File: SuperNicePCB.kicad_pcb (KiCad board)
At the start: 4 copper layers, 100 x 100 mm, 59 parts, among them J1 UART Debug, J2 Boot Opt, SW1 Reset, U1 ESP32-S3-WROOM-1-N8, U2 SY8089AAAC, U3 SGM2048-ADJXTEK8G/TR, U4 ICS-43434_C5656610, U5 AM312, U6 SCD40-D-R1, U7 SHT40-AD1B-R3, U8 HLK-LD6002, U9 DWM3000TR13

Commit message: Problems
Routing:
- net /HumanSesors/3.3V: track 299.4 -> 109.6 mm
- net /MCU/VDD33: track 131.2 -> 32.9 mm
- net /MCU/BOOT: track 77.2 -> 25.7 mm, vias 1 -> 0
- net GND: track 331.5 -> 298.1 mm, vias 35 -> 31
- net /PIR_OUT: track 32.9 -> 29.1 mm
- net /TEMP_SCL: track 75.8 -> 74.3 mm
- removed copper zone on In2.Cu, net /HumanSesors/3.3V

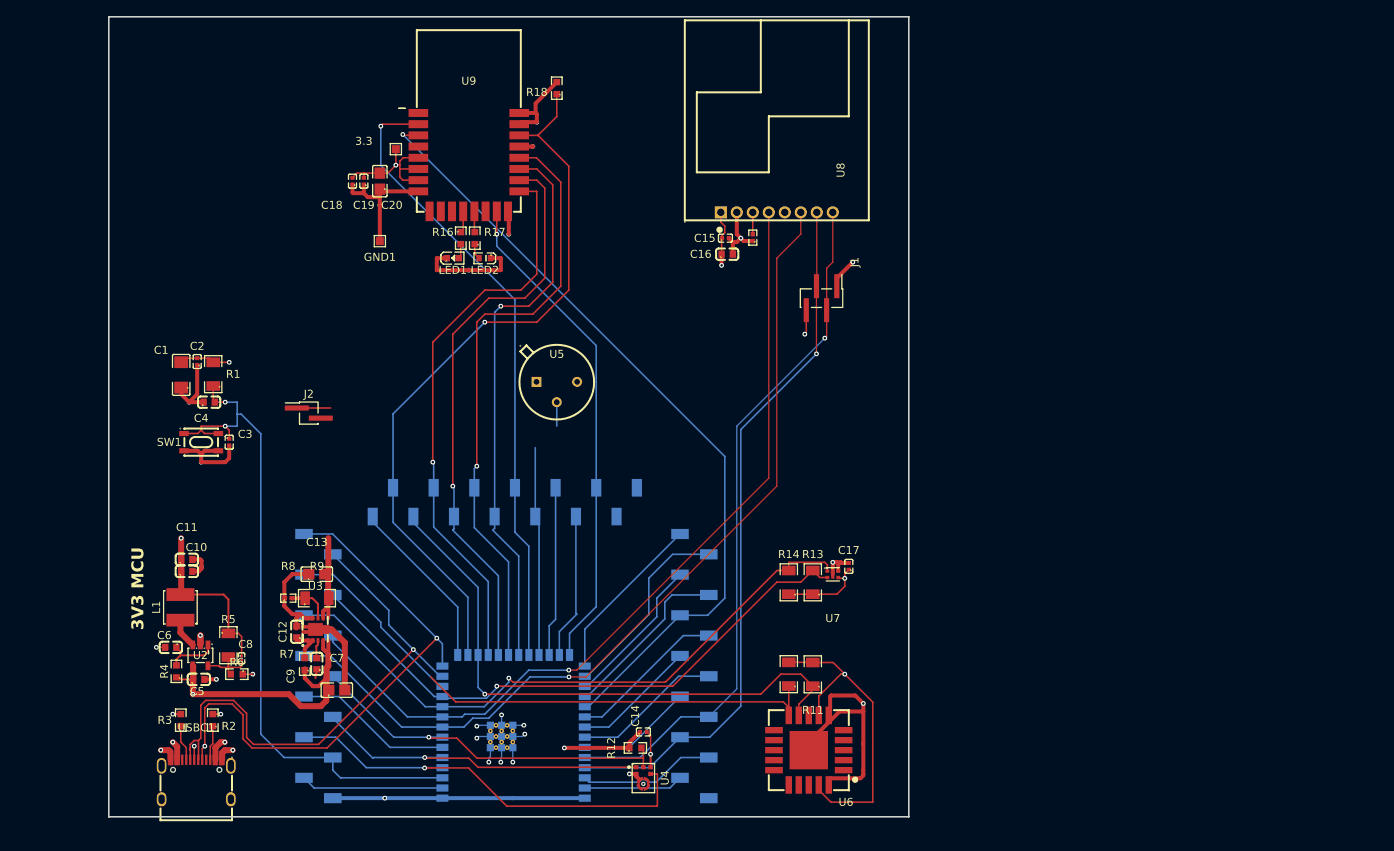
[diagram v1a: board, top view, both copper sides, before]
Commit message: Power error correction/ redo of the wiring
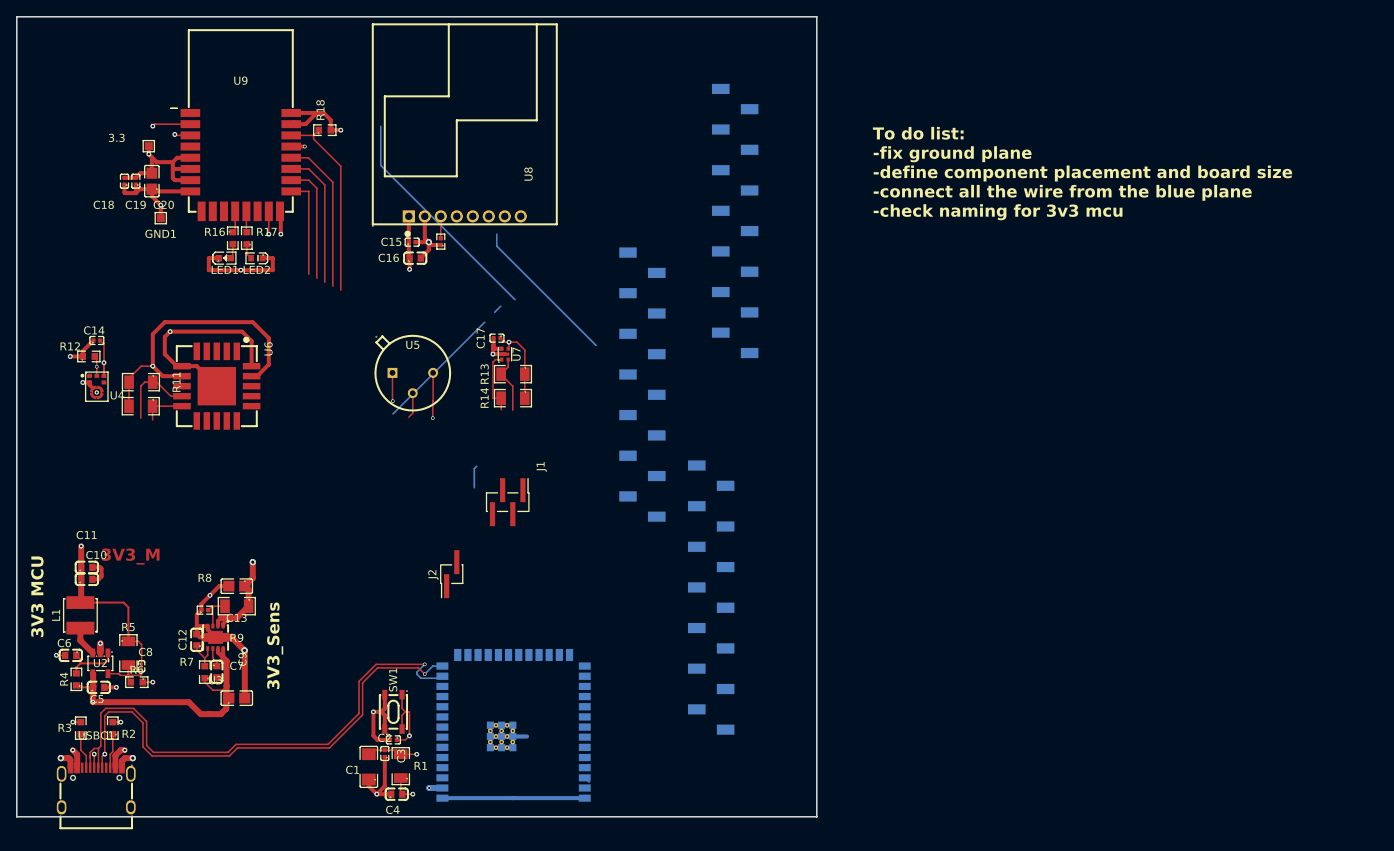
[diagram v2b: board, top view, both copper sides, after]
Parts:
- moved R11 91.6 mm to (96.5, 95.5), turned to 180 degrees
- moved R10 87.7 mm to (96.5, 98.5), turned to 180 degrees
- moved U6 86.9 mm to (106.0, 96.0), turned to -90 degrees
- moved C14 84.0 mm to (91.0, 90.3)
- moved R12 84.0 mm to (90.0, 92.3)
- moved U4 84.0 mm to (91.0, 96.0)
- moved H1 76.2 mm to (170.8, 75.3)
- moved C1 54.3 mm to (125.0, 143.6)
- moved C4 54.3 mm to (128.5, 147.0)
- moved R1 54.3 mm to (129.0, 143.5)
- moved C2 54.3 mm to (127.0, 141.9)
- moved C17 52.4 mm to (141.0, 90.0), turned to 180 degrees
- moved U7 49.4 mm to (142.0, 92.0), turned to 90 degrees
- moved J1 46.8 mm to (142.4, 110.5)
- moved R13 45.6 mm to (143.0, 94.5), turned to 180 degrees
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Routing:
- net /HumanSesors/3.3V: track 109.6 -> 252.2 mm, vias 5 -> 7
- net /HumanSesors/U0_RTS: track 110.7 -> 0.00 mm, vias 1 -> 0
- net /HumanSesors/U0_CTS: track 104.8 -> 0.00 mm, vias 1 -> 0
- net /MCU/UWB_RST: track 99.8 -> 2.46 mm
- net /MCU/TXD: track 88.4 -> 0.00 mm, vias 1 -> 0
- net /MCU/RXD: track 87.1 -> 0.00 mm, vias 1 -> 0
- net GND: track 298.1 -> 224.6 mm, vias 31 -> 23
- net /MCU/EN: track 86.8 -> 13.3 mm
- net /TEMP_SDA: track 79.8 -> 8.21 mm, vias 1 -> 0
- net /HumanSesors/C02_SDA: track 73.9 -> 5.90 mm
- net /TEMP_SCL: track 74.3 -> 7.58 mm, vias 1 -> 0
- net /HumanSesors/CO2_SCL: track 73.1 -> 10.3 mm, vias 1 -> 0
- net /MCU/UWB_CS0: track 71.0 -> 12.5 mm, vias 1 -> 0
- net /MCU/UWB_MOSI: track 71.8 -> 14.9 mm, vias 1 -> 0
- net /HumanSesors/AC_BCLK: track 54.8 -> 0.00 mm, vias 1 -> 0
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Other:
- board text added: "3V3_M"
- board text added: "3V3_Sens"
- board text added: "To do list: -fix ground plane -define component placement and board size -connect all the wire from the blue plane -check naming for 3v3 mcu"

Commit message: Rerouting
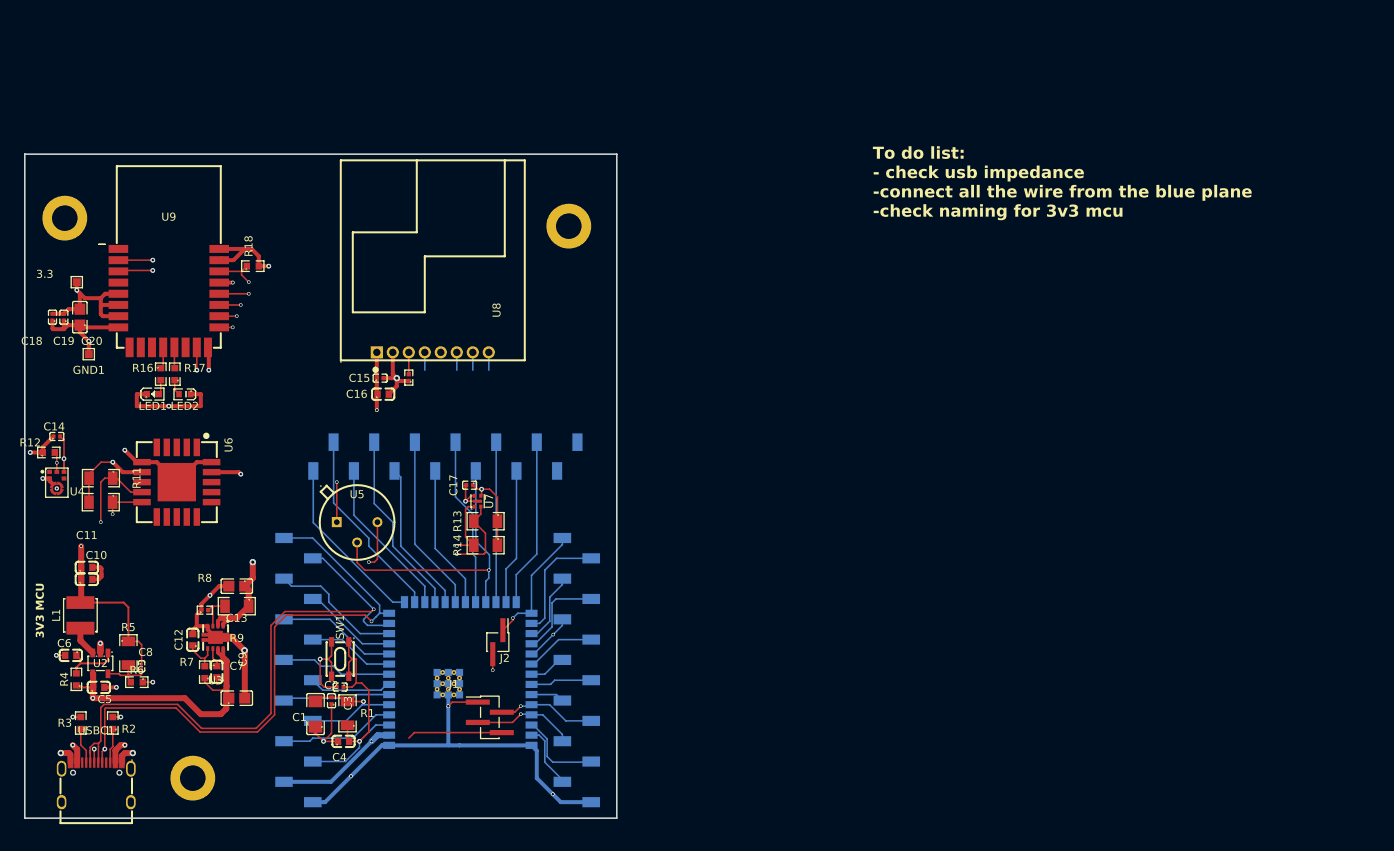
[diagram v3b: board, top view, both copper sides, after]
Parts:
- added REF**: MountingHole_3.2mm_M3_DIN965_Pad, MountingHole:MountingHole_3.2mm_M3_DIN965_Pad, F.Cu at (150.0, 76.0)
- added REF**: MountingHole_3.2mm_M3_DIN965_Pad, MountingHole:MountingHole_3.2mm_M3_DIN965_Pad, F.Cu at (103.0, 145.0)
- added REF**: MountingHole_3.2mm_M3_DIN965_Pad, MountingHole:MountingHole_3.2mm_M3_DIN965_Pad, F.Cu at (87.0, 75.0)
- moved H1 78.3 mm to (116.2, 131.5)
- moved J1 27.0 mm to (140.1, 137.4), turned to 0 degrees
- moved H2 26.2 mm to (134.6, 104.8), turned to 180 degrees
- moved U5 19.9 mm to (123.5, 114.3)
- moved 3.3 19.2 mm to (88.5, 83.0)
- moved C18 19.2 mm to (85.5, 87.4)
- moved C19 19.2 mm to (86.9, 87.4)
- moved C20 19.2 mm to (88.9, 87.4)
- moved GND1 19.2 mm to (90.0, 92.0)
- moved LED1 19.2 mm to (98.0, 97.0)
- moved LED2 19.2 mm to (102.0, 97.0)
- moved R16 19.2 mm to (99.0, 94.5)
- moved R17 19.2 mm to (100.8, 94.5)
- moved R18 19.2 mm to (110.5, 81.0)
- moved U9 19.2 mm to (100.0, 85.0)
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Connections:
- C1 pad 2: /MCU/VDD33 -> /MCU/3V3_MCU
- C10 pad 1: /MCU/VDD33 -> /MCU/3V3_MCU
- C11 pad 1: /MCU/VDD33 -> /MCU/3V3_MCU
- C2 pad 2: /MCU/VDD33 -> /MCU/3V3_MCU
- C8 pad 1: /MCU/VDD33 -> /MCU/3V3_MCU
- H1 pad 13: Net-(U1-3V3) -> /MCU/3V3_MCU
- L1 pad 2: /MCU/VDD33 -> /MCU/3V3_MCU
- R1 pad 2: /MCU/VDD33 -> /MCU/3V3_MCU
- R5 pad 1: /MCU/VDD33 -> /MCU/3V3_MCU
- U1 pad 2: Net-(U1-3V3) -> /MCU/3V3_MCU
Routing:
- net /MCU/3V3_MCU: track 0.00 -> 113.2 mm, vias 0 -> 3
- net Net-(U1-3V3): track 63.8 -> 0.00 mm, vias 1 -> 0
- net /HumanSesors/3.3V: track 252.2 -> 188.6 mm, vias 7 -> 8
- net /PIR_OUT: track 3.21 -> 36.7 mm, vias 0 -> 1
- net GND: track 224.6 -> 247.1 mm, vias 23 -> 27
- net /MCU/IO3: track 0.00 -> 22.0 mm
- net /HumanSesors/CO2_SCL: track 10.3 -> 31.4 mm, vias 0 -> 1
- net /MCU/EN: track 13.3 -> 34.0 mm, vias 2 -> 1
- net /MCU/IO47: track 0.00 -> 20.0 mm
- net /MCU/IO48: track 0.00 -> 16.9 mm
- net /MCU/VDD33: track 28.6 -> 11.9 mm, vias 2 -> 0
- net /HumanSesors/U0_RTS: track 0.00 -> 16.1 mm
- net /HumanSesors/C02_SDA: track 5.90 -> 21.9 mm, vias 0 -> 1
- net /MCU/BOOT: track 0.00 -> 15.6 mm, vias 0 -> 1
- net /MCU/TXD: track 0.00 -> 15.1 mm, vias 0 -> 1
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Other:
- board size 100 x 100 mm -> 74 x 83 mm
- board text added: "To do list: - check usb impedance -connect all the wire from the blue plane -check naming for 3v3 mcu"
- board text removed: "3V3_M"
- board text removed: "3V3_Sens"
- board text removed: "To do list: -fix ground plane -define component placement and board size -connect all the wire from the blue plane -check naming for 3v3 mcu"

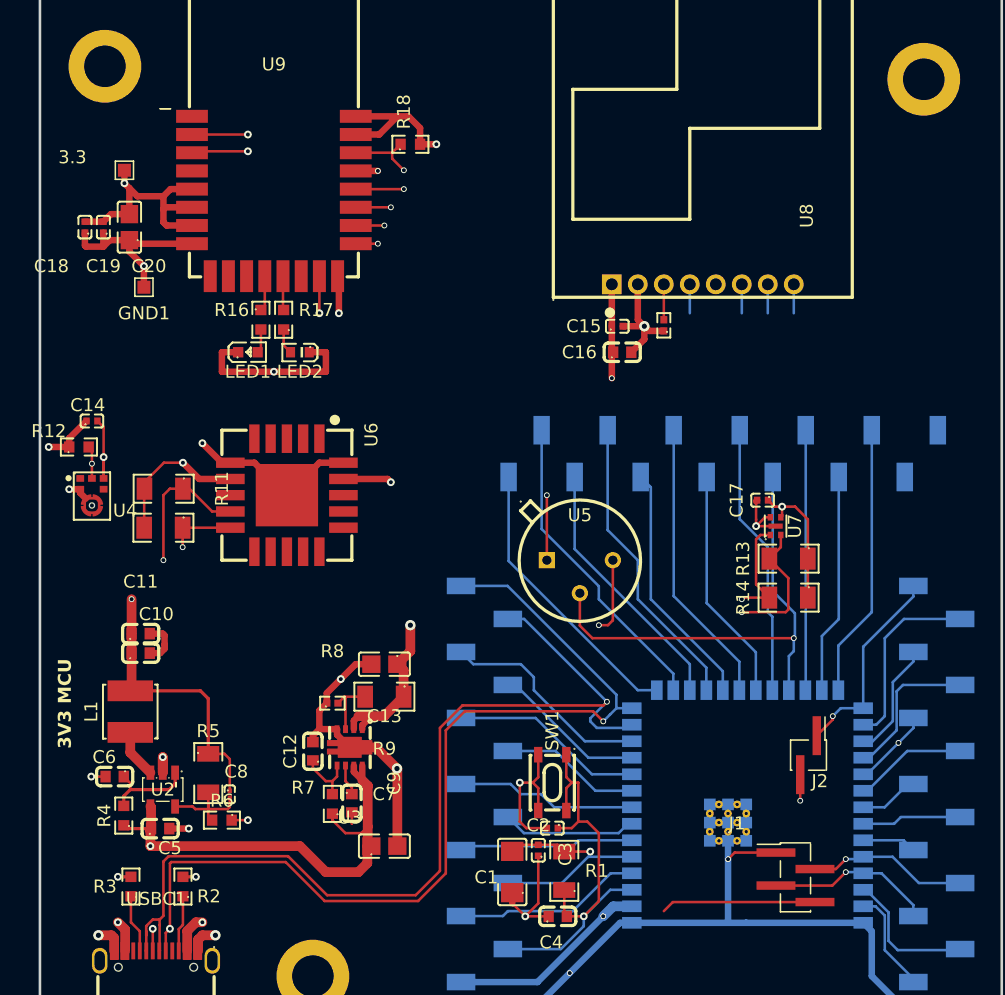
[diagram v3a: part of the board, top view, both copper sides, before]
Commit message: Wired MCU IO
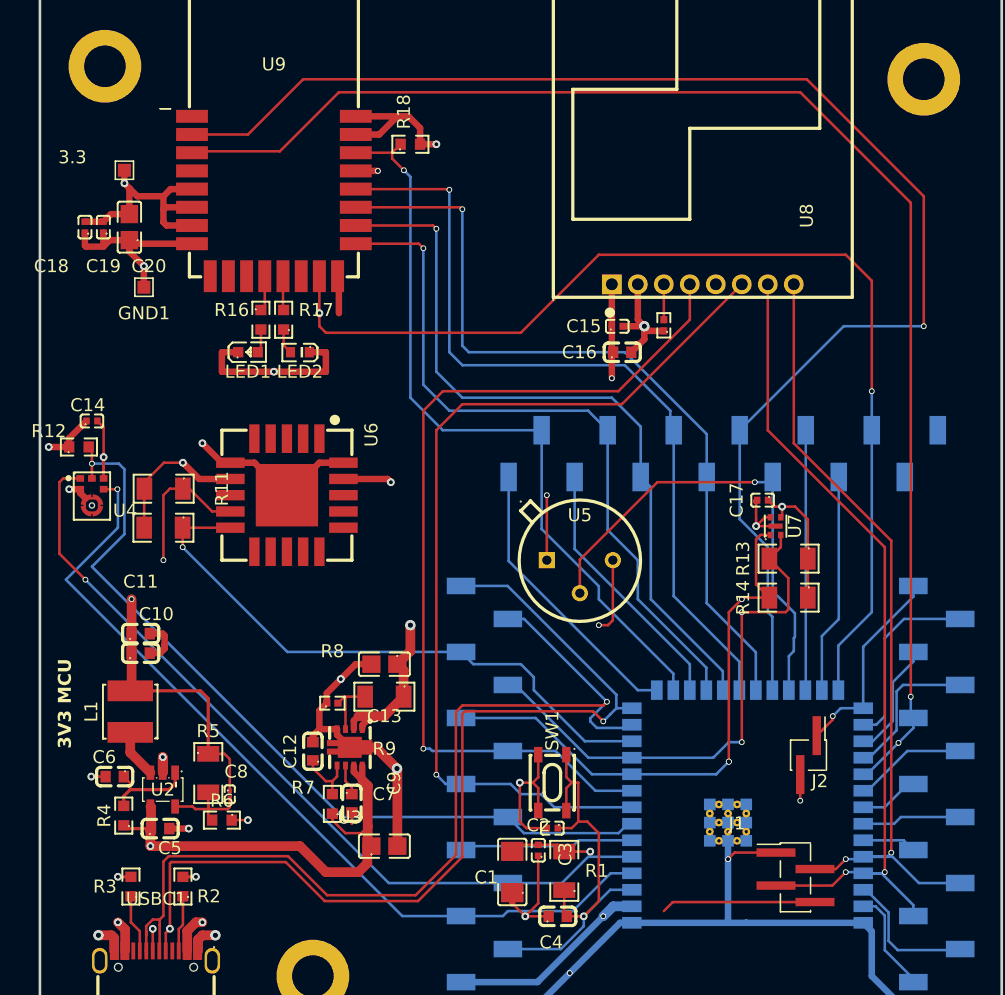
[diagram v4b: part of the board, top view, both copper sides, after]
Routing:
- net /MCU/UWB_RST: track 10.8 -> 106.9 mm
- net /MCU/UWB_WAKEUP: track 25.4 -> 110.3 mm
- net /MCU/UWB_RXOK: track 23.9 -> 82.4 mm, vias 1 -> 2
- net /HumanSesors/U0_CTS: track 13.0 -> 69.5 mm, vias 0 -> 1
- net /HumanSesors/U0_RTS: track 16.1 -> 70.7 mm, vias 0 -> 1
- net /HumanSesors/AC_LRCLK: track 10.4 -> 62.6 mm, vias 0 -> 1
- net /HumanSesors/DIN: track 12.9 -> 64.1 mm
- net /HumanSesors/AC_BCLK: track 14.5 -> 65.4 mm, vias 0 -> 1
- net /MCU/TXD: track 15.1 -> 63.5 mm, vias 1 -> 2
- net /MCU/RXD: track 14.6 -> 61.5 mm, vias 1 -> 2
- net /MCU/UWB_MISO: track 21.4 -> 62.3 mm
- net /MCU/UWB_SCK: track 25.8 -> 62.3 mm
- net /MCU/UWB_MOSI: track 21.2 -> 57.7 mm
- net /MCU/UWB_CS0: track 24.8 -> 54.6 mm
- net /MCU/UWB_IRQ: track 30.3 -> 59.2 mm
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
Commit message: Ready for DRC
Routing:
- net /HumanSesors/CO2_SCL: track 31.4 -> 71.9 mm, vias 1 -> 3
- net GND: vias 26 -> 27
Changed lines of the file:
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@@
 	)
 	(via blind
+		(at 105 94)
+		(size 0.45)
+		(drill 0.3)
+		(layers "F.Cu" "In1.Cu")
+		(net "GND")
+	)
+	(via blind
 		(at 84.25 107.54)
 		(size 0.6)
@@
 	)
 	(segment
+		(start 119 104)
+		(end 114.5 108.5)
+		(width 0.2)
+		(layer "F.Cu")
+		(net "/HumanSesors/CO2_SCL")
+	)
+	(segment
+		(start 123 104)
+		(end 119 104)
+		(width 0.2)
+		(layer "F.Cu")
+		(net "/HumanSesors/CO2_SCL")
+	)
+	(segment
+		(start 91.5 113)
+		(end 94 115.5)
+		(width 0.2)
+		(layer "F.Cu")
+		(net "/HumanSesors/CO2_SCL")
+	)
+	(segment
+		(start 94 115.5)
+		(end 108.5 115.5)
+		(width 0.2)
+		(layer "F.Cu")
+		(net "/HumanSesors/CO2_SCL")
+	)
+	(segment
 		(start 91.5 113)
 		(end 91.5 108)
@@
 	)
 	(via
-		(at 91.5 113)
+		(at 123 104)
+		(size 0.45)
+		(drill 0.3)
+		(layers "F.Cu" "B.Cu")
+		(net "/HumanSesors/CO2_SCL")
+	)
+	(via
+		(at 114.5 108.5)
+		(size 0.45)
+		(drill 0.3)
+		(layers "F.Cu" "B.Cu")
+		(net "/HumanSesors/CO2_SCL")
+	)
+	(via
+		(at 108.5 115.5)
 		(size 0.45)
 		(drill 0.3)
@@
 	)
 	(segment
+		(start 123.14 106.6)
+		(end 123.14 104.14)
+		(width 0.2)
+		(layer "B.Cu")
+		(net "/HumanSesors/CO2_SCL")
+	)
+	(segment
 		(start 123.14 112.14)
 		(end 123.14 106.6)
@@
 	)
 	(segment
+		(start 123.14 104.14)
+		(end 123 104)
+		(width 0.2)
+		(layer "B.Cu")
+		(net "/HumanSesors/CO2_SCL")
+	)
+	(segment
+		(start 114.5 109.5)
+		(end 114.5 108.5)
+		(width 0.2)
+		(layer "B.Cu")
+		(net "/HumanSesors/CO2_SCL")
+	)
+	(segment
+		(start 108.5 115.5)
+		(end 114.5 109.5)
+		(width 0.2)
+		(layer "B.Cu")
+		(net "/HumanSesors/CO2_SCL")
+	)
+	(segment
 		(start 123.54 115.54)
 		(end 123.54 112.96)
@@
 		)
 		(min_thickness 0.25)
-		(fill
+		(fill yes
 			(thermal_gap 0.5)
 			(thermal_bridge_width 0.5)

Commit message: Fixed som DRC error
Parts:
- added 3.4: TestPoint, TestPoint:TestPoint_Pad_1.0x1.0mm, F.Cu at (91.2, 116.0)
- added 3.5: TestPoint, TestPoint:TestPoint_Pad_1.0x1.0mm, F.Cu at (100.0, 116.0)
- added 3.6: TestPoint, TestPoint:TestPoint_Pad_1.0x1.0mm, F.Cu at (108.8, 116.2)
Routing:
- net /HumanSesors/3.3V: track 188.6 -> 191.8 mm, vias 8 -> 9
- net GND: track 247.1 -> 250.3 mm, vias 27 -> 32
- net /MCU/3V3_MCU: track 113.2 -> 115.4 mm, vias 3 -> 4
- net /HumanSesors/CO2_SCL: track 71.9 -> 70.7 mm

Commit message: DRC
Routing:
- net GND: track 250.3 -> 247.5 mm
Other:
- board size 74 x 83 mm -> 75 x 85 mm

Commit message: DRC issues solved
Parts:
- moved REF** 3.25 mm to (150.0, 72.8)
- moved REF** 3.13 mm to (105.8, 146.5)
- moved REF** 1.82 mm to (87.5, 73.2)
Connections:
- H2 pad 2: unconnected-(H2-Pad2) -> GND
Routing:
- net GND: track 247.5 -> 250.3 mm, vias 32 -> 34
- net /HumanSesors/CO2_SCL: track 70.7 -> 72.7 mm
